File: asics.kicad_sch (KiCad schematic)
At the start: 0 parts

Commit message: schematic done, started initial placement
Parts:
- added J3: 2x9P 2mm, emberone:CONN-TH_X2026WV-2-09D-46SN, symbol Connector_Generic:Conn_02x09_Odd_Even
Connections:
- new net 3V3: J3.16 (Pin_16)
- new net A0: J3.8 (Pin_8)
- new net A1: J3.7 (Pin_7)
- new net A2: J3.6 (Pin_6)
- new net GND: J3.1 (Pin_1), J3.10 (Pin_10), J3.13 (Pin_13), J3.14 (Pin_14), J3.2 (Pin_2), J3.9 (Pin_9)
- new net PLUG: J3.5 (Pin_5)
- new net RST: J3.15 (Pin_15)
- new net RXD: J3.12 (Pin_12)
- new net SCL: J3.4 (Pin_4)
- new net SDA: J3.3 (Pin_3)
- new net TXD: J3.11 (Pin_11)
- no-connect marks 0 -> 2

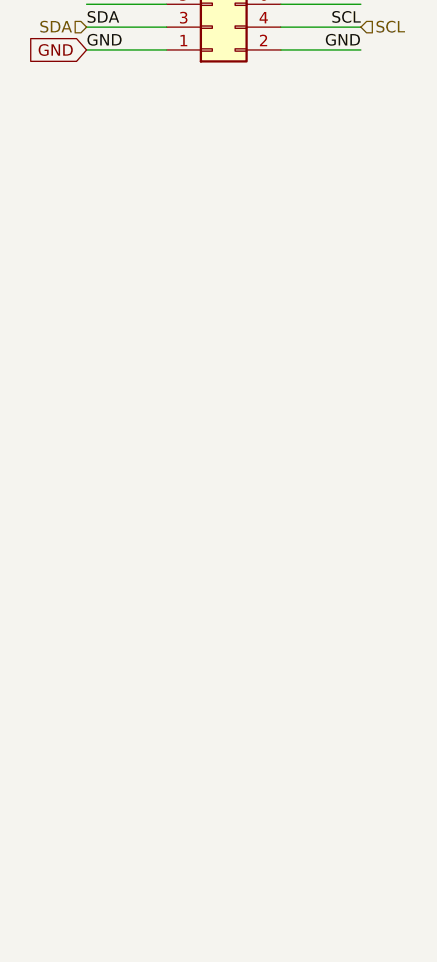
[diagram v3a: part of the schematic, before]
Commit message: added BM1362AC symbol and footprint
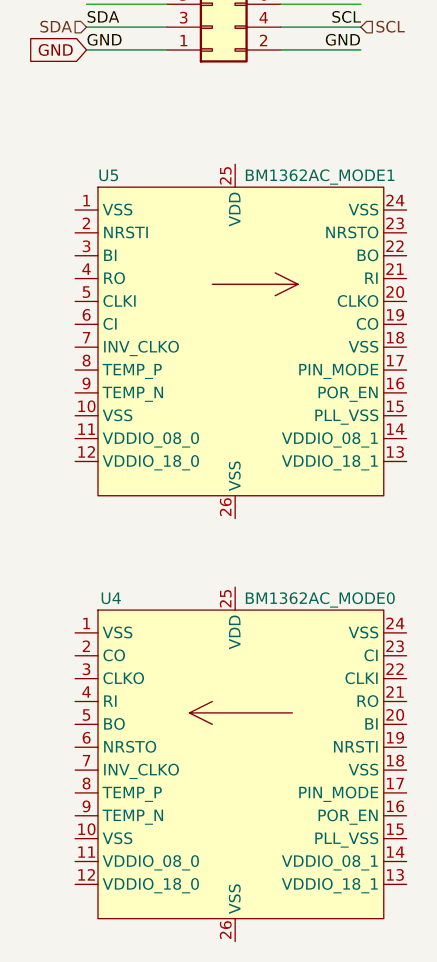
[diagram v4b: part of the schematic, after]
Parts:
- added U4: BM1362AC_MODE0, emberone:BM1362AC, symbol emberone:BM1362AC_MODE0
- added U5: BM1362AC_MODE1, emberone:BM1362AC, symbol emberone:BM1362AC_MODE1
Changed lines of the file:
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@@
+		)
+	)
+	(symbol
+		(lib_id "emberone:BM1362AC_MODE1")
+		(at 186.69 81.28 0)
+		(unit 1)
+		(exclude_from_sim no)
+		(in_bom yes)
+		(on_board yes)
+		(dnp no)
+		(property "Reference" "U5"
+			(at 171.45 63.5 0)
+			(effects
+				(font
+					(size 1.27 1.27)
+				)
+				(justify left)
+			)
+		)
+		(property "Value" "BM1362AC_MODE1"
+			(at 187.706 63.5 0)
+			(effects
+				(font
+					(size 1.27 1.27)
+				)
+				(justify left)
+			)
+		)
+		(property "Footprint" "emberone:BM1362AC"
+			(at 199.898 103.886 0)
+			(effects
+				(font
+					(size 1.27 1.27)
+				)
+				(hide yes)
+			)
+		)
+		(property "Datasheet" ""
+			(at 196.85 77.47 0)
+			(effects
+				(font
+					(size 1.27 1.27)
+				)
+				(hide yes)
+			)
+		)
+		(property "Description" ""
+			(at 196.85 77.47 0)
+			(effects
+				(font
+					(size 1.27 1.27)
+				)
+				(hide yes)
+			)
+		)
+		(pin "12"
+		)
+		(pin "16"
+		)
+		(pin "10"
+		)
+		(pin "14"
+		)
+		(pin "5"
+		)
+		(pin "11"
+		)
+		(pin "24"
+		)
+		(pin "26"
+		)
+		(pin "13"
+		)
+		(pin "25"
+		)
+		(pin "8"
+		)
+		(pin "23"
+		)
+		(pin "22"
+		)
+		(pin "17"
+		)
+		(pin "19"
+		)
+		(pin "21"
+		)
+		(pin "3"
+		)
+		(pin "2"
+		)
+		(pin "20"
+		)
+		(pin "9"
+		)
+		(pin "4"
+		)
+		(pin "7"
+		)
+		(pin "6"
+		)
+		(pin "15"
+		)
+		(pin "18"
+		)
+		(pin "1"
+		)
+		(instances
+			(project ""
+				(path "/b036224c-4cdf-48cc-81df-19bc5283ebd2/8fbe5865-2681-4e3d-9bfe-f9d833280d6f"
+					(reference "U5")
+					(unit 1)
+				)
+			)
+		)
+	)
+	(symbol
+		(lib_id "emberone:BM1362AC_MODE0")
+		(at 186.69 128.27 0)
+		(unit 1)
+		(exclude_from_sim no)
+		(in_bom yes)
+		(on_board yes)
+		(dnp no)
+		(property "Reference" "U4"
+			(at 171.704 110.49 0)
+			(effects
+				(font
+					(size 1.27 1.27)
+				)
+				(justify left)
+			)
+		)
+		(property "Value" "BM1362AC_MODE0"
+			(at 187.706 110.49 0)
+			(effects
+				(font
+					(size 1.27 1.27)
+				)
+				(justify left)
+			)
+		)
+		(property "Footprint" "emberone:BM1362AC"
+			(at 198.882 147.574 0)
+			(effects
+				(font
+					(size 1.27 1.27)
+				)
+				(hide yes)
+			)
+		)
+		(property "Datasheet" ""
+			(at 196.85 124.46 0)
+			(effects
+				(font
+					(size 1.27 1.27)
+				)
+				(hide yes)
+			)
+		)
+		(property "Description" ""
+			(at 196.85 124.46 0)
+			(effects
+				(font
+					(size 1.27 1.27)
+				)
+				(hide yes)
+			)
+		)
+		(pin "10"
+		)
+		(pin "13"
+		)
+		(pin "14"
+		)
+		(pin "2"
+		)
+		(pin "20"
+		)
+		(pin "21"
+		)
+		(pin "22"
+		)
+		(pin "23"
+		)
+		(pin "24"
+		)
+		(pin "25"
+		)
+		(pin "12"
+		)
+		(pin "11"
+		)
+		(pin "15"
+		)
+		(pin "16"
+		)
+		(pin "17"
+		)
+		(pin "18"
+		)
+		(pin "19"
+		)
+		(pin "26"
+		)
+		(pin "3"
+		)
+		(pin "4"
+		)
+		(pin "5"
+		)
+		(pin "6"
+		)
+		(pin "7"
+		)
+		(pin "8"
+		)
+		(pin "9"
+		)
+		(pin "1"
+		)
+		(instances
+			(project ""
+				(path "/b036224c-4cdf-48cc-81df-19bc5283ebd2/8fbe5865-2681-4e3d-9bfe-f9d833280d6f"
+					(reference "U4")
+					(unit 1)
+				)
+			)
 		)
 	)

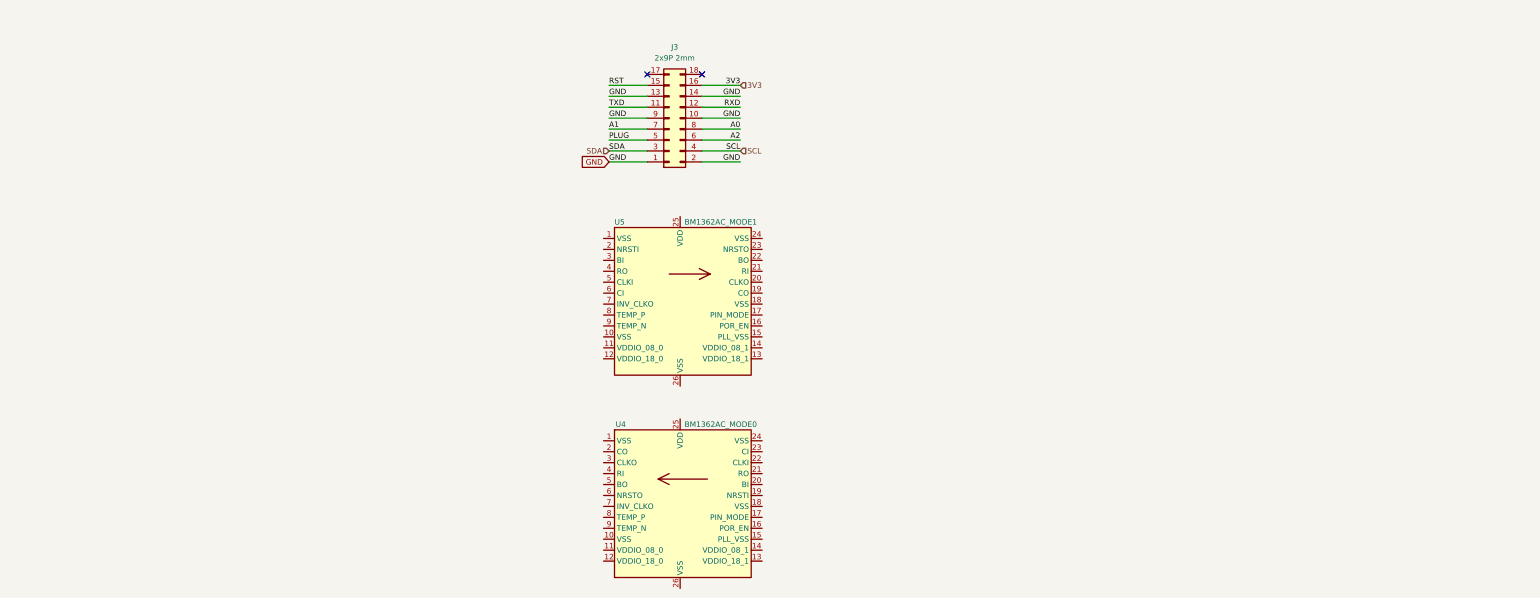
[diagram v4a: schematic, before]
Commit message: adding initial ASIC stacks
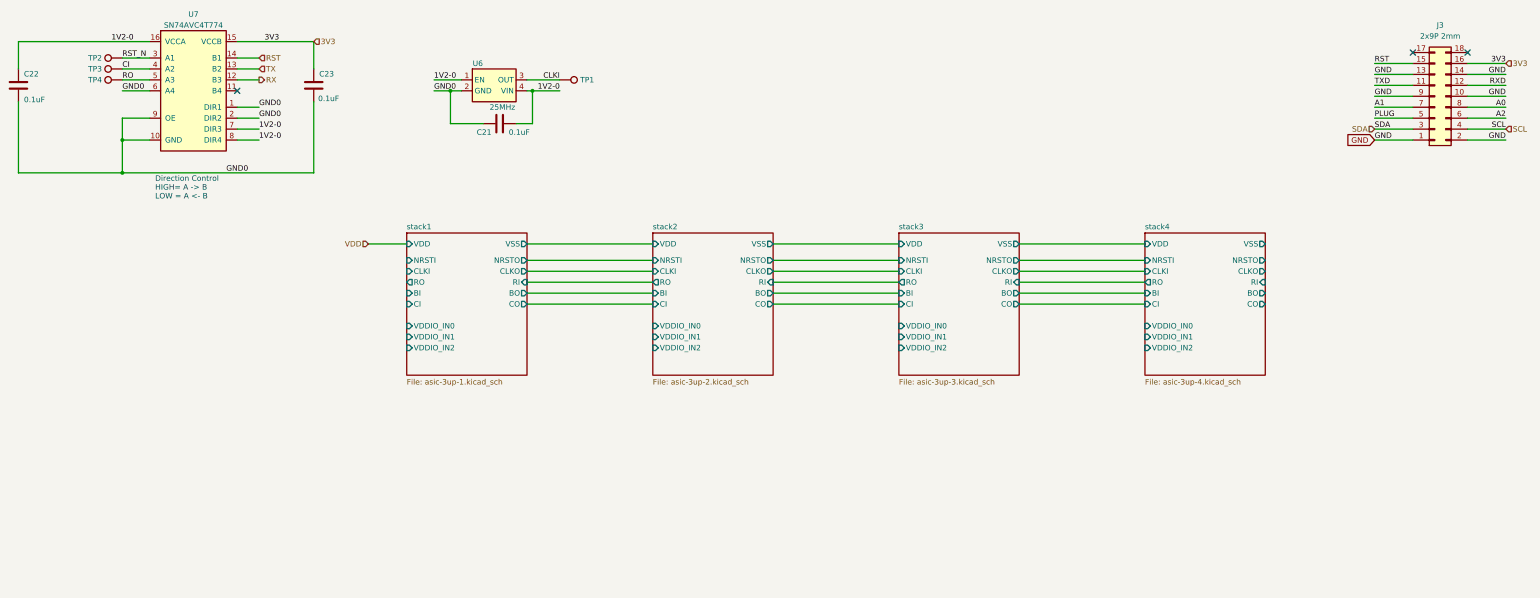
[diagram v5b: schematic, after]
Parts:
- removed U4: BM1362AC_MODE0, emberone:BM1362AC, symbol emberone:BM1362AC_MODE0
- removed U5: BM1362AC_MODE1, emberone:BM1362AC, symbol emberone:BM1362AC_MODE1
- added C21, C22, C23: 0.1uF, Capacitor_SMD:C_0402_1005Metric, symbol Device:C
- added TP1, TP2, TP3, TP4: TestPoint, TestPoint:TestPoint_Pad_D1.5mm, symbol Connector:TestPoint
- added U6: 25MHz, bitaxe:SMD3225-4P, symbol bitaxe:oscillator
- added U7: SN74AVC4T774, Package_SO:TSSOP-16_4.4x5mm_P0.65mm, symbol bitaxe:SN74AVC4T774
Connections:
- net 3V3: now also C23.1, U7.15 (VCCB)
- net RST: now also U7.14 (B1)
- new net 1V2-0: C21.2, C22.1, U6.1 (EN), U6.4 (VIN), U7.16 (VCCA), U7.7 (DIR3), U7.8 (DIR4)
- new net CI: TP3.1, U7.4 (A2)
- new net CLKI: TP1.1, U6.3 (OUT)
- new net GND0: C21.1, C22.2, C23.2, U6.2 (GND), U7.1 (DIR1), U7.10 (GND), U7.2 (DIR2), U7.6 (A4), U7.9 (OE)
- new net RO: TP4.1, U7.5 (A3)
- new net RST_N: TP2.1, U7.3 (A1)
- new net RX: U7.12 (B3)
- new net TX: U7.13 (B2)
- no-connect marks 2 -> 3
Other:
- added sheet stack1 (asic-3up-1.kicad_sch)
- added sheet stack2 (asic-3up-2.kicad_sch)
- added sheet stack3 (asic-3up-3.kicad_sch)
- added sheet stack4 (asic-3up-4.kicad_sch)
- note added: "Direction Control HIGH= A -> B LOW = A <- B"
- moved on the sheet: J3

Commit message: added all the ASICs to the schematic. added the RP2040 circuit for data. added the VDDIO boost circuit. schematic cleanup
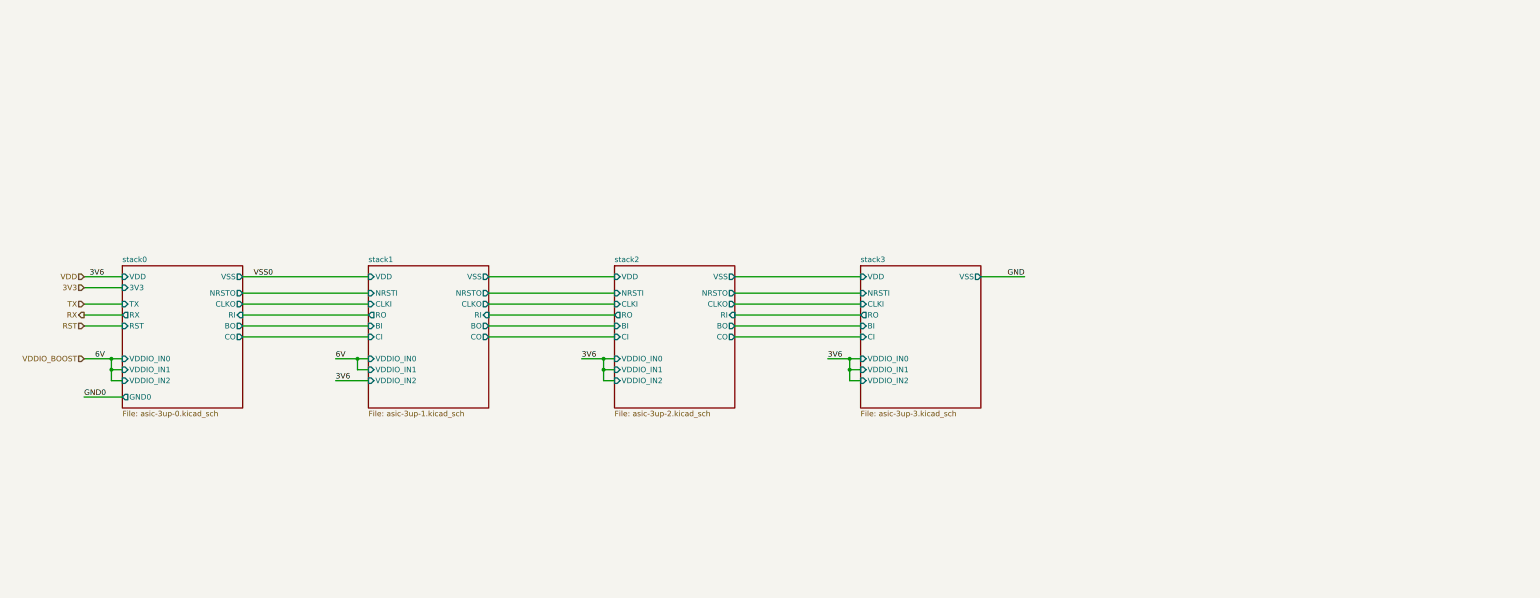
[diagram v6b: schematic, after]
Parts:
- removed C21, C22, C23: 0.1uF, Capacitor_SMD:C_0402_1005Metric, symbol Device:C
- removed J3: 2x9P 2mm, emberone:CONN-TH_X2026WV-2-09D-46SN, symbol Connector_Generic:Conn_02x09_Odd_Even
- removed TP1, TP2, TP3, TP4: TestPoint, TestPoint:TestPoint_Pad_D1.5mm, symbol Connector:TestPoint
- removed U6: 25MHz, bitaxe:SMD3225-4P, symbol bitaxe:oscillator
- removed U7: SN74AVC4T774, Package_SO:TSSOP-16_4.4x5mm_P0.65mm, symbol bitaxe:SN74AVC4T774
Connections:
- no-connect marks 3 -> 0
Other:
- removed sheet stack4
- added sheet stack0 (asic-3up-0.kicad_sch)
- sheet stack3 ports: added none; removed BO, CLKO, CO, NRSTO, RI
- note removed: "Direction Control HIGH= A -> B LOW = A <- B"

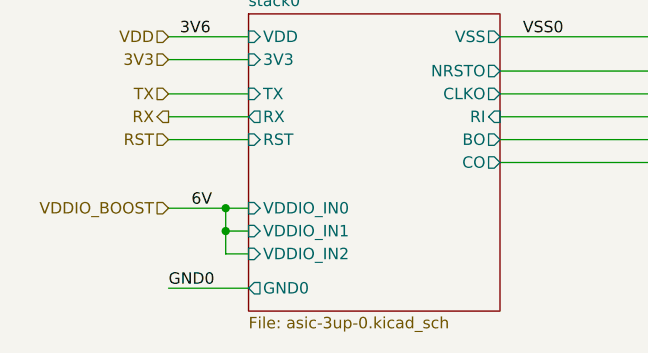
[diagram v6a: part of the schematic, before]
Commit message: added sweet logo to schematic worksheet. Schematic cleanup.
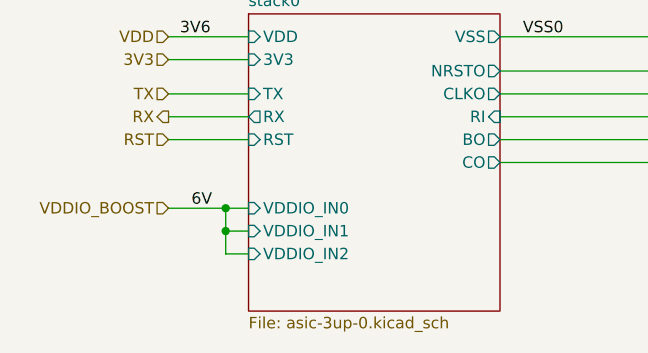
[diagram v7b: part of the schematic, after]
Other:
- sheet stack0 ports: added none; removed GND0
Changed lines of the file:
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@@
 	(generator "eeschema")
 	(generator_version "8.0")
-	(paper "A4")
+	(paper "A3")
 	(title_block
 		(date "2024-11-25")
@@
 	(wire
 		(pts
-			(xy 48.26 104.14) (xy 57.15 104.14)
-		)
-		(stroke
-			(width 0)
-			(type default)
-		)
-	)
-	(wire
-		(pts
 			(xy 142.24 85.09) (xy 171.45 85.09)
 		)
@@
 	(label "VSS0"
 		(at 87.63 76.2 0)
-		(fields_autoplaced yes)
-		(effects
-			(font
-				(size 1.27 1.27)
-			)
-			(justify left bottom)
-		)
-	)
-	(label "GND0"
-		(at 48.26 104.14 0)
 		(fields_autoplaced yes)
 		(effects
@@
 			(effects
 				(font
-					(size 1.27 1.27)
-				)
-				(justify left)
-			)
-		)
-		(pin "GND0" output
-			(at 57.15 104.14 180)
-			(effects
-				(font
